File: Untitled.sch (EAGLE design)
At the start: 22 parts, among them IC1 ILD4001, IC2 ILD4001, IC3 ILD4001, IC4 74AHC1G125DBV, IC5 74AHC1G125DBV, U1 ATMEGA328P

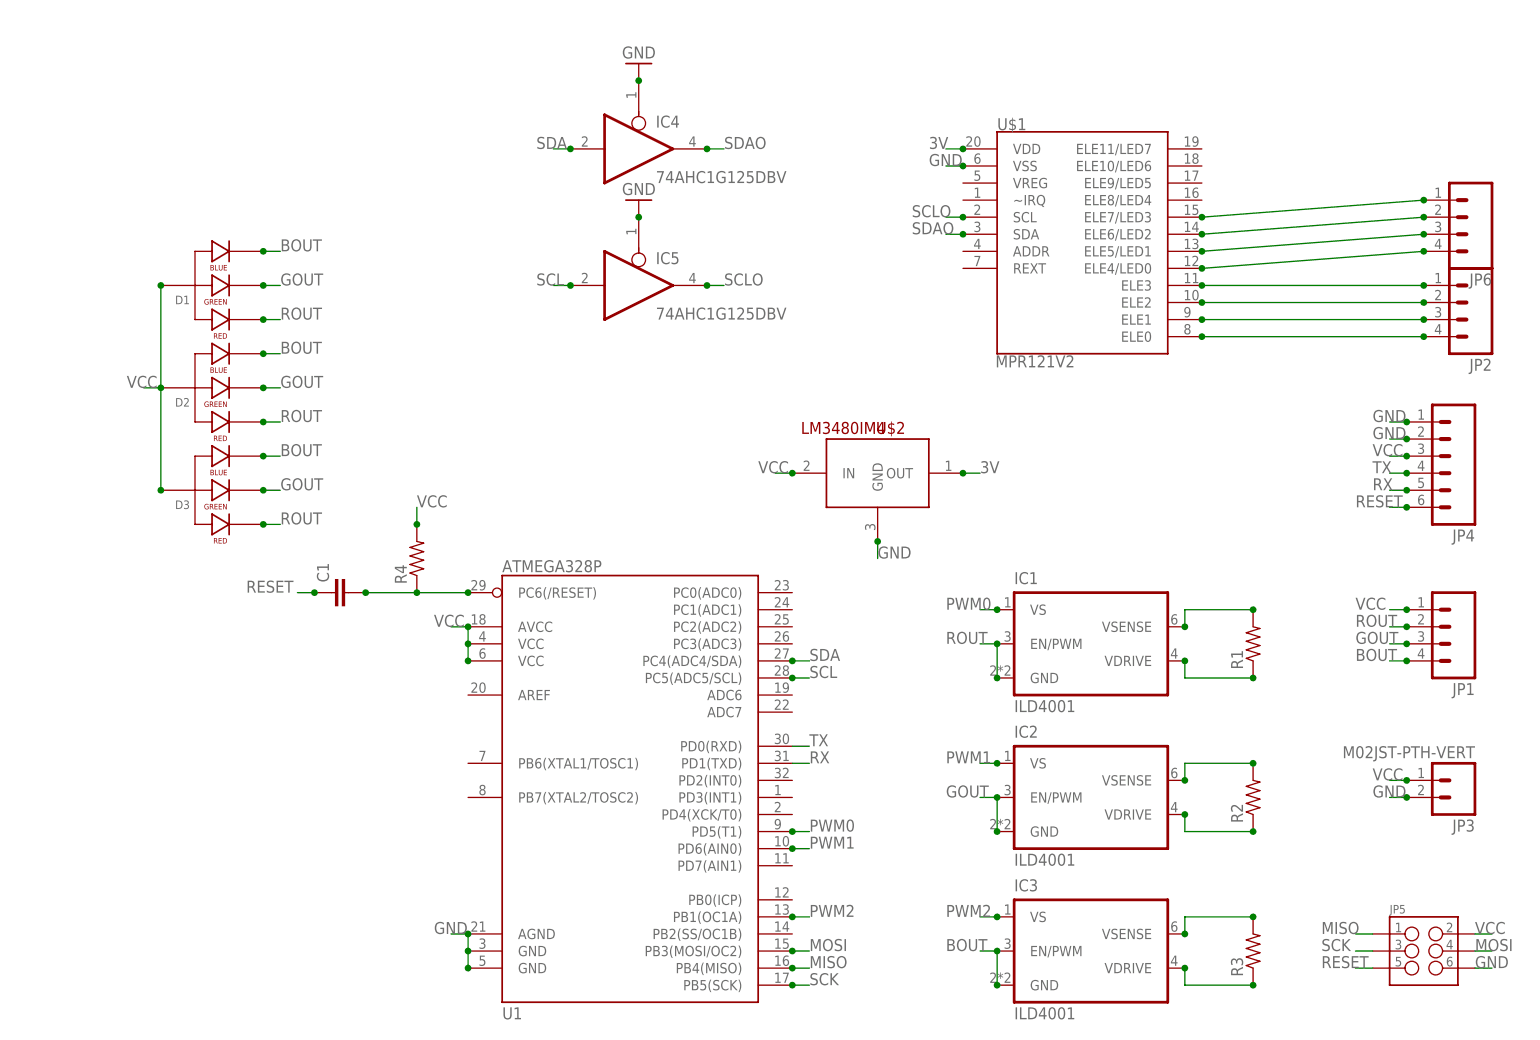
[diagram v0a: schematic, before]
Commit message: Fixed unidirectional buffer and added missing connections to mpr121
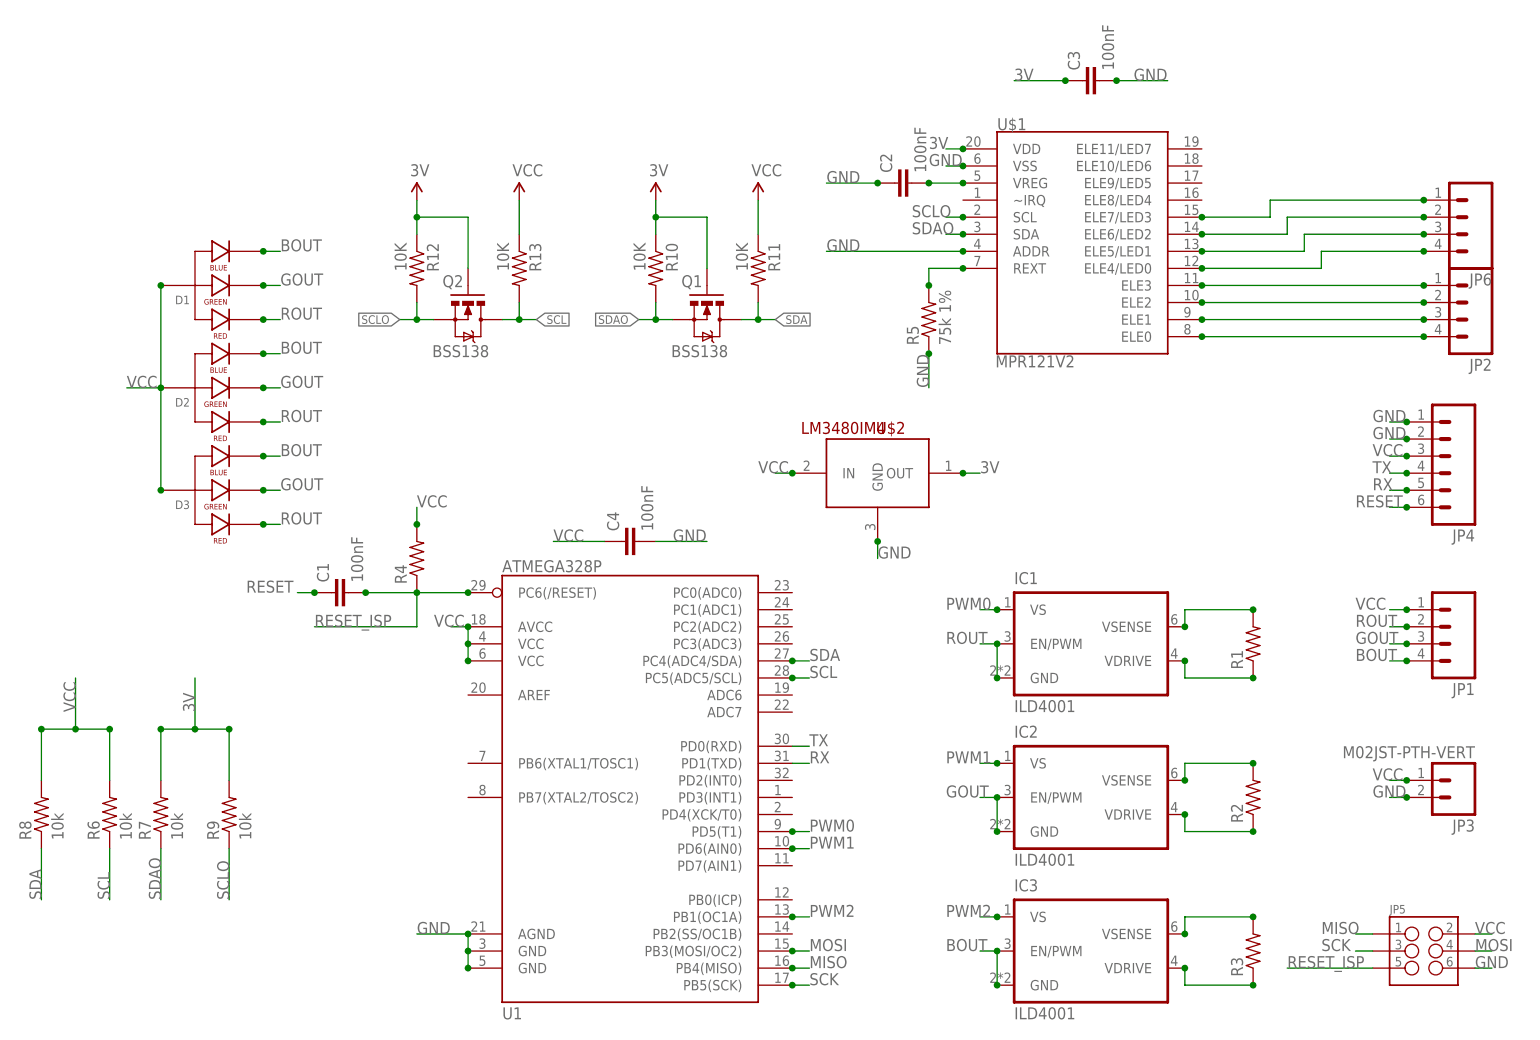
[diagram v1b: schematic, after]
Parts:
- removed IC4, IC5: 74AHC1G125DBV, 74xx-little-us:74AHC1G125DBV
- added C2, C3, C4: 100nF, SparkFun-Capacitors:CAP0805
- added Q1, Q2: BSS138, SparkFun:MOSFET-NCHANNELSMD
- added R10, R11, R12, R13: 10K, SparkFun:RESISTOR0603-RES
- added R5: 75k 1%, SparkFun-Resistors:RESISTOR0805-RES
- added R6, R7, R8, R9: 10k, SparkFun-Resistors:RESISTOR0805-RES
- C1: value (none) -> 100nF
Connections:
- removed net N$5 (its old number): C1.2, R4.1, U1.PC6(/RESET)
- new net N$16: R5.2, U$1.REXT
- new net N$17: C2.2, U$1.VREG
- new net RESET_ISP: C1.2, JP5.5, R4.1, U1.PC6(/RESET)
- net 3V: now also C3.1, Q1.G, Q2.G, R10.1, R12.1, R7.2, R9.2
- net GND: now also C2.1, C3.2, C4.2, R5.1, U$1.ADDR; no longer IC4A.OE, IC5A.OE
- net RESET: no longer JP5.5
- net SCL: now also Q2.D, R13.2, R6.1; no longer IC5A.I
- net SCLO: now also Q2.S, R12.2, R9.1; no longer IC5A.O
- net SDA: now also Q1.D, R11.2, R8.1; no longer IC4A.I
- net SDAO: now also Q1.S, R10.2, R7.1; no longer IC4A.O
- net VCC: now also C4.1, R11.1, R13.1, R6.2, R8.2
